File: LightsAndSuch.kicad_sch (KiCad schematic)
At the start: 13 parts, among them U1 STM32F205RBTx, U2 MAX98357A

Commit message: added secondary circuit
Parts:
- removed C10, C11, C12, C13, C14, C9: 100n, symbol Device:C
- removed C15: 1u, symbol Device:C
- removed C16: 4.7u', symbol Device:C
- removed C17: 0.1u, symbol Device:C
- removed C18: 10u, symbol Device:C
- removed LS1: Speaker, symbol Device:Speaker
- removed U1: STM32F205RBTx, Package_QFP:LQFP-64_10x10mm_P0.5mm, symbol MCU_ST_STM32F2:STM32F205RBTx
- removed U2: MAX98357A, Package_DFN_QFN:TQFN-16-1EP_3x3mm_P0.5mm_EP1.23x1.23mm, symbol Audio:MAX98357A
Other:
- added sheet Primary Sound Circuit (PrimarySoundCircuit.kicad_sch)
- added sheet Secondary Sound Circuit (SecondarySoundCircuit.kicad_sch)
- sheet TPS54202 ports: added none; removed 5V
- sheet TPS57A20 ports: added none; removed 3.3v, 5V

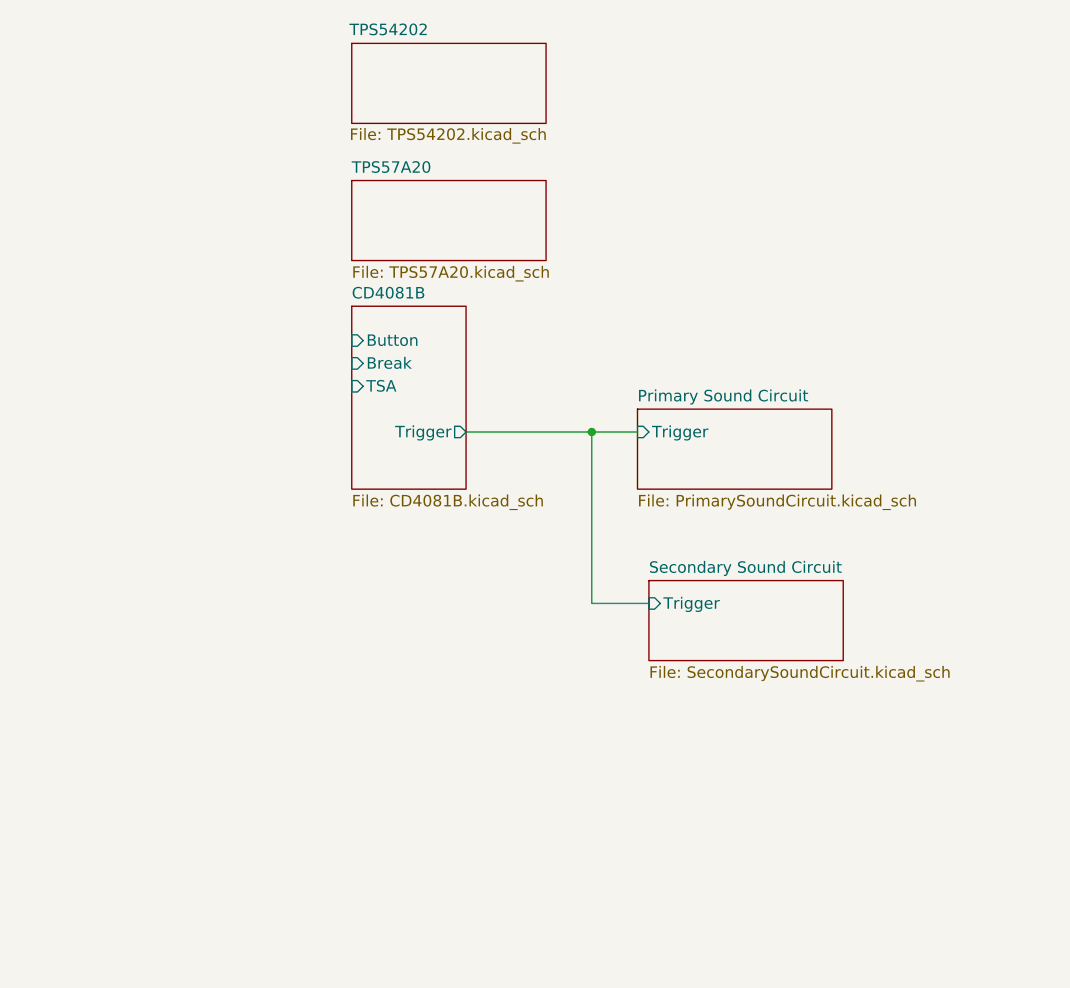
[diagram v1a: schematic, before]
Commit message: finished lights
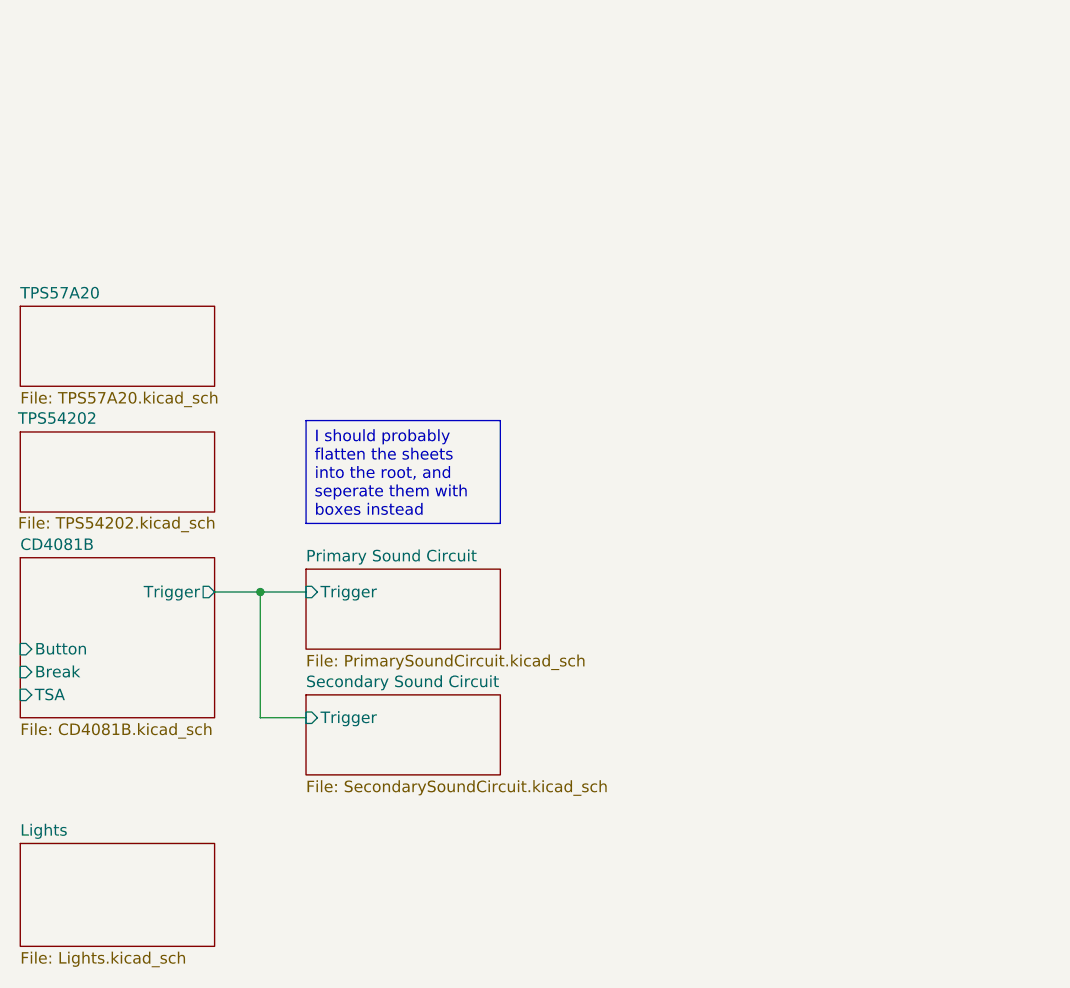
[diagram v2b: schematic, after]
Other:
- added sheet Lights (Lights.kicad_sch)
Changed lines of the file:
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@@
 	(generator_version "9.0")
 	(paper "A4")
+	(text_box "I should probably flatten the sheets into the root, and seperate them with boxes instead "
+		(exclude_from_sim no)
+		(at 76.2 59.69 0)
+		(size 21.59 11.43)
+		(margins 0.9525 0.9525 0.9525 0.9525)
+		(stroke
+			(width 0)
+			(type solid)
+		)
+		(fill
+			(type none)
+		)
+		(effects
+			(font
+				(size 1.27 1.27)
+			)
+			(justify left top)
+		)
+	)
 	(junction
-		(at 107.95 60.96)
+		(at 71.12 78.74)
 		(diameter 0)
 		(color 0 0 0 0)
@@
 	(wire
 		(pts
-			(xy 107.95 80.01) (xy 114.3 80.01)
+			(xy 71.12 92.71) (xy 76.2 92.71)
 		)
 		(stroke
@@
 	(wire
 		(pts
-			(xy 107.95 60.96) (xy 107.95 80.01)
+			(xy 66.04 78.74) (xy 71.12 78.74)
 		)
 		(stroke
@@
 	(wire
 		(pts
-			(xy 107.95 60.96) (xy 113.03 60.96)
+			(xy 71.12 92.71) (xy 71.12 78.74)
 		)
 		(stroke
@@
 	(wire
 		(pts
-			(xy 93.98 60.96) (xy 107.95 60.96)
+			(xy 71.12 78.74) (xy 76.2 78.74)
 		)
 		(stroke
@@
 	)
 	(sheet
-		(at 114.3 77.47)
+		(at 76.2 90.17)
 		(size 21.59 8.89)
 		(exclude_from_sim no)
@@
 		)
 		(property "Sheetname" "Secondary Sound Circuit"
-			(at 114.3 76.7584 0)
+			(at 76.2 89.4584 0)
 			(effects
 				(font
@@
 		)
 		(property "Sheetfile" "SecondarySoundCircuit.kicad_sch"
-			(at 114.3 86.9446 0)
+			(at 76.2 99.6446 0)
 			(effects
 				(font
@@
 		)
 		(pin "Trigger" input
-			(at 114.3 80.01 180)
+			(at 76.2 92.71 180)
 			(effects
 				(font
@@
 	)
 	(sheet
-		(at 81.28 46.99)
-		(size 12.7 20.32)
+		(at 44.45 74.93)
+		(size 21.59 17.78)
 		(exclude_from_sim no)
 		(in_bom yes)
@@
 		)
 		(property "Sheetname" "CD4081B"
-			(at 81.28 46.2784 0)
+			(at 44.45 74.2184 0)
 			(effects
 				(font
@@
 		)
 		(property "Sheetfile" "CD4081B.kicad_sch"
-			(at 81.28 67.8946 0)
+			(at 44.45 93.2946 0)
 			(effects
 				(font
@@
 		)
 		(pin "Button" input
-			(at 81.28 50.8 180)
+			(at 44.45 85.09 180)
 			(effects
 				(font
@@
 		)
 		(pin "Trigger" output
-			(at 93.98 60.96 0)
+			(at 66.04 78.74 0)
 			(effects
 				(font
@@
 		)
 		(pin "Break" input
-			(at 81.28 53.34 180)
+			(at 44.45 87.63 180)
 			(effects
 				(font
@@
 		)
 		(pin "TSA" input
-			(at 81.28 55.88 180)
+			(at 44.45 90.17 180)
 			(effects
 				(font
@@
 	)
 	(sheet
-		(at 81.28 17.78)
+		(at 44.45 60.96)
 		(size 21.59 8.89)
 		(exclude_from_sim no)
@@
 		)
 		(property "Sheetname" "TPS54202"
-			(at 81.026 17.018 0)
+			(at 44.196 60.198 0)
 			(effects
 				(font
@@
 		)
 		(property "Sheetfile" "TPS54202.kicad_sch"
-			(at 81.026 27.178 0)
+			(at 44.196 70.358 0)
 			(effects
 				(font
@@
 	)
 	(sheet
-		(at 81.28 33.02)
+		(at 44.45 46.99)
 		(size 21.59 8.89)
 		(exclude_from_sim no)
@@
 		)
 		(property "Sheetname" "TPS57A20"
-			(at 81.28 32.3084 0)
+			(at 44.45 46.2784 0)
 			(effects
 				(font
@@
 		)
 		(property "Sheetfile" "TPS57A20.kicad_sch"
-			(at 81.28 42.4946 0)
+			(at 44.45 56.4646 0)
 			(effects
 				(font
@@
 	)
 	(sheet
-		(at 113.03 58.42)
+		(at 76.2 76.2)
 		(size 21.59 8.89)
 		(exclude_from_sim no)
@@
 		)
 		(property "Sheetname" "Primary Sound Circuit"
-			(at 113.03 57.7084 0)
+			(at 76.2 75.4884 0)
 			(effects
 				(font
@@
 		)
 		(property "Sheetfile" "PrimarySoundCircuit.kicad_sch"
-			(at 113.03 67.8946 0)
+			(at 76.2 85.6746 0)
 			(effects
 				(font
@@
 		)
 		(pin "Trigger" input
-			(at 113.03 60.96 180)
+			(at 76.2 78.74 180)
 			(effects
 				(font
@@
 				)
 			)
+		)
+	)
+	(sheet
+		(at 44.45 106.68)
+		(size 21.59 11.43)
+		(exclude_from_sim no)
+		(in_bom yes)
+		(on_board yes)
+		(dnp no)
+		(fields_autoplaced yes)
+		(stroke
+			(width 0.1524)
+			(type solid)
+		)
+		(fill
+			(color 0 0 0 0.0000)
+		)
+		(property "Sheetname" "Lights"
+			(at 44.45 105.9684 0)
+			(effects
+				(font
+					(size 1.27 1.27)
+				)
+				(justify left bottom)
+			)
+		)
+		(property "Sheetfile" "Lights.kicad_sch"
+			(at 44.45 118.6946 0)
+			(effects
+				(font
+					(size 1.27 1.27)
+				)
+				(justify left top)
+			)
+		)
+		(instances
+			(project "LightsAndSuch"
+				(path "/f2987657-b7e0-480f-b307-23af9e47acd8"
+					(page "7")
+				)
+			)

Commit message: flattened file into one sheet
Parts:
- added 0.1u: Cboot, symbol Device:C_Small
- added C1: 10u, symbol Device:C_Small
- added C10, C11, C12, C13, C14, C9: 100n, symbol Device:C
- added C15, C2, C7, C8: 1u, symbol Device:C
- added C16: 4.7u', symbol Device:C
- added C17, C19, C23, C25: 0.1u, symbol Device:C
- added C18, C22, C24: 10u, symbol Device:C
- added C20: 0.01u, symbol Device:C
- added C21, C26, C27: C, symbol Device:C
- added C3, C5: 22u, symbol Device:C
- added C4: 0.1u, symbol Device:C_Small
- added C6: 75p, symbol Device:C
- added D1, D2, D3: LED, symbol Device:LED
- added L1: 20u, symbol Device:L_Iron
- added LS1: Speaker, symbol Device:Speaker
- added LS2, LS3: MSO206NR, symbol Device:Speaker
- added Q1: AO3400A, Package_TO_SOT_SMD:SOT-23, symbol Transistor_FET:AO3400A
- added Q2: NPN, symbol Simulation_SPICE:NPN
- added R1, R10, R11, R12, R13, R14, R15, R16, R17, R3, R9: R, symbol Device:R
- added R2: 100k, symbol Device:R_Small
- added R4: 100k, symbol Device:R
- added R5: 13.3k, symbol Device:R_Small
- added R6: 5.23k, symbol Device:R_Small
- added R7: 13.7k, symbol Device:R_Small
- added R8: 100, symbol Device:R
- added U1: STM32F205RBTx, Package_QFP:LQFP-64_10x10mm_P0.5mm, symbol MCU_ST_STM32F2:STM32F205RBTx
- added U2: MAX98357A, Package_DFN_QFN:TQFN-16-1EP_3x3mm_P0.5mm_EP1.23x1.23mm, symbol Audio:MAX98357A
- added U3: TPS54202DDC, Package_TO_SOT_SMD:SOT-23-6, symbol Regulator_Switching:TPS54202DDC
- added U4: TPS7A20xxxDQN, Package_SON:Texas_X2SON-4_1x1mm_P0.65mm, symbol Regulator_Linear:TPS7A20xxxDQN
- added U5: CD4081BM, D14, symbol CD4081B:CD4081BM
- added U6, U7, U8: LM555xM, Package_SO:SOIC-8_3.9x4.9mm_P1.27mm, symbol Timer:LM555xM
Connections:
- new net: R10.2, R9.1, U7.7 (DIS)
- new net: 0.1u.2, L1.1, U3.2 (SW)
- new net: C6.2, R2.2, R5.1, U3.4 (FB)
- new net: 0.1u.1, U3.6 (BOOT)
- new net: Q2.2 (B), R15.1
- new net: R1.2, U6.7 (DIS)
- new net: D2.2 (A), U8.3 (Q)
- new net: C27.1, U8.5 (CV)
- new net: R13.2, R14.1, U8.7 (DIS)
- new net: R8.1, U6.3 (Q)
- new net: Q1.1 (G), R4.1, R8.2
- new net: D1.2 (A), U7.3 (Q)
- new net: Q2.1 (C), R16.1, R17.2
- new net: U1.34 (PB13), U2.16 (BCLK)
- new net: U1.36 (PB15), U2.1 (DIN)
- new net: U1.62 (PB9), U2.14 (LRCLK)
- new net: LS2.2, LS3.2, Q1.3 (D)
- new net: D3.2 (A), R17.1
- new net: C26.1, U7.5 (CV)
- new net: U5.3 (J), U5.5 (C)
- new net: R7.1, U5.4 (K)
- new net: C20.1, U6.5 (CV)
- new net: LS1.1, U2.9 (OUTP)
- new net: LS1.2, U2.10 (OUTN)
- new net +12V: C1.1, C4.1, R10.1, R13.1, R16.2, U3.3 (VIN), U5.14 (VDD), U7.8 (VCC), U8.8 (VCC)
- new net +3.3V: C10.1, C11.1, C12.1, C13.1, C14.2, C15.2, C16.1, C8.1, C9.1, U1.1 (VBAT), U1.13 (VDDA), U1.19 (VDD), U1.32 (VDD), U1.48 (VDD), U1.64 (VDD), U2.4 (~{SD_MODE}), U4.1 (OUT)
- new net +5V: C17.2, C18.2, C19.1, C19.2, C2.1, C2.2, C21.2, C22.1, C22.2, C23.1, C23.2, C24.1, C24.2, C25.1, C25.2, C3.1, C5.1, C6.1, C7.1, L1.2, LS2.1, LS3.1, R1.1, R2.1, U2.2 (GAIN_SLOT), U2.7 (VDD), U2.8 (VDD), U4.3 (EN), U4.4 (IN), U6.6 (THR), U6.8 (VCC)
- new net Break: U5.2 (B)
- new net Button: U5.6 (D)
- new net FAULT: R12.1, R15.2, U8.4 (R)
- new net GND: C1.2, C10.2, C11.2, C12.2, C13.2, C14.1, C15.1, C16.2, C17.1, C18.1, C20.2, C21.1, C26.2, C27.2, C3.2, C4.2, C5.2, C7.2, C8.2, C9.2, D1.1 (K), D2.1 (K), D3.1 (K), Q1.2 (S), Q2.3 (E), R11.2, R12.2, R14.2, R3.1, R4.2, R5.2, R6.2, R9.2, U1.12 (VSSA), U1.18 (VSS), U1.63 (VSS), U2.11 (GND), U2.15 (GND), U2.17 (PAD), U2.3 (GND), U3.1 (GND), U4.2 (GND), U4.5 (Pad), U5.7 (VSS), U6.1 (GND), U6.4 (R), U7.1 (GND), U7.2 (TR), U7.6 (THR), U8.1 (GND), U8.2 (TR), U8.6 (THR)
- new net HV_Enable: R11.1, U7.4 (R)
- new net TSA: U5.1 (A)
- new net Trigger: R3.2, R6.1, R7.2, U1.8 (PC0), U6.2 (TR)
- no-connect marks 0 -> 1
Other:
- removed sheet CD4081B
- removed sheet Lights
- removed sheet Primary Sound Circuit
- removed sheet Secondary Sound Circuit
- removed sheet TPS54202
- removed sheet TPS57A20
- note added: "Lights"
- note added: "Logic"
- note added: "Power"
- note added: "Primary Sound Circuit"
- note added: "Secondary Sound Circuit"

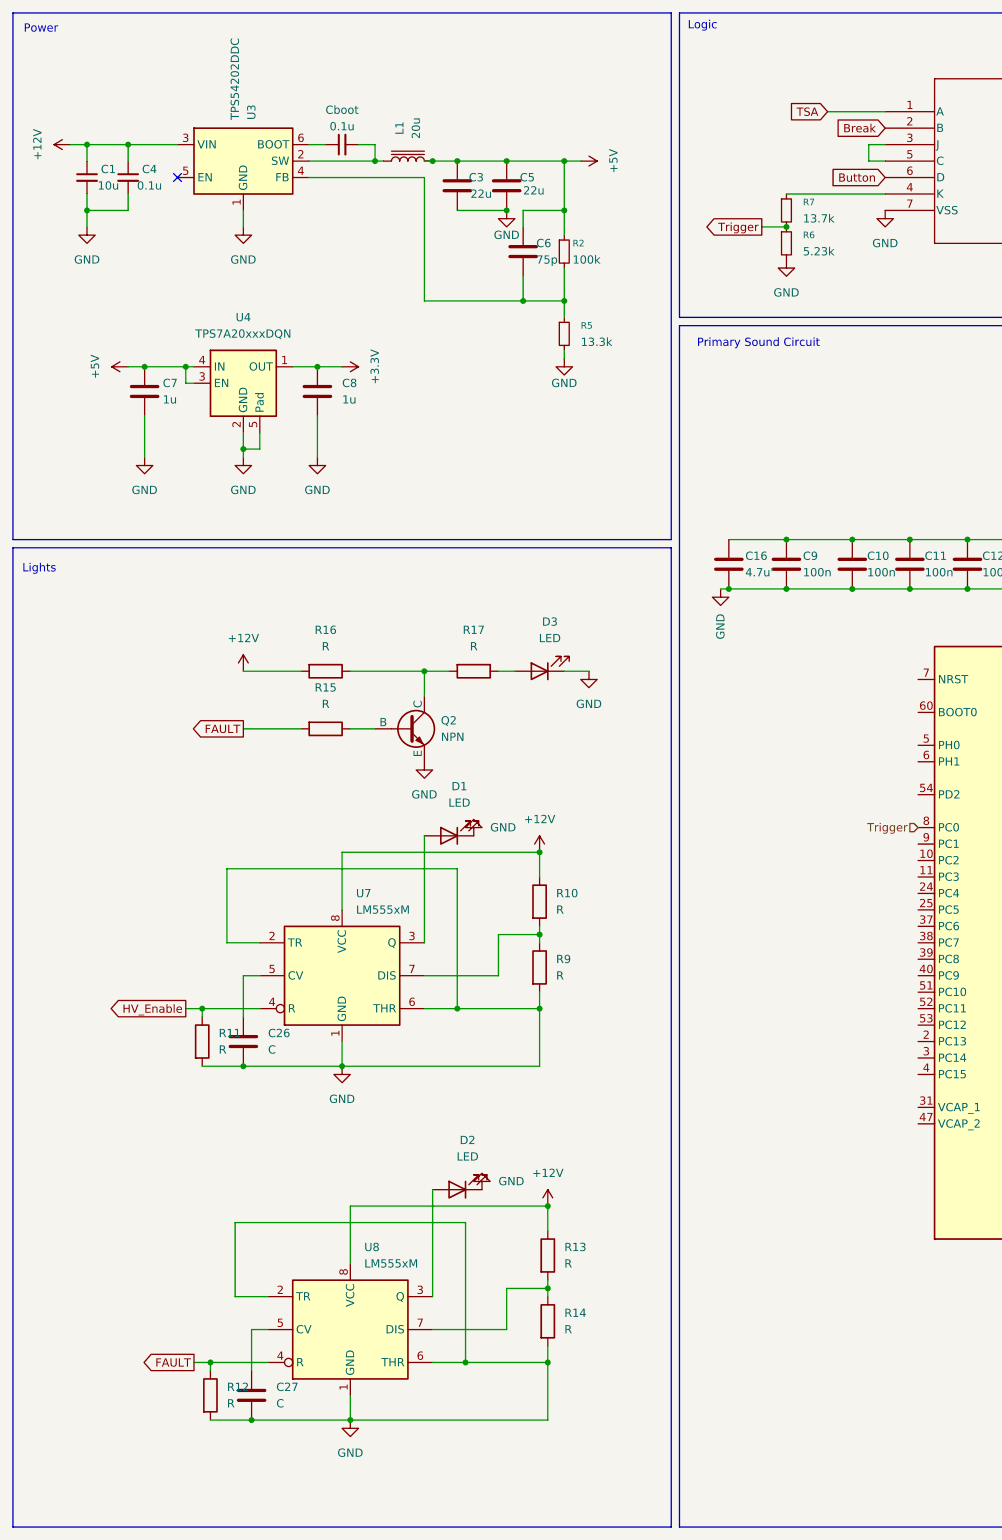
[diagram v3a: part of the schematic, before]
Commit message: added missing capacitor for the 555
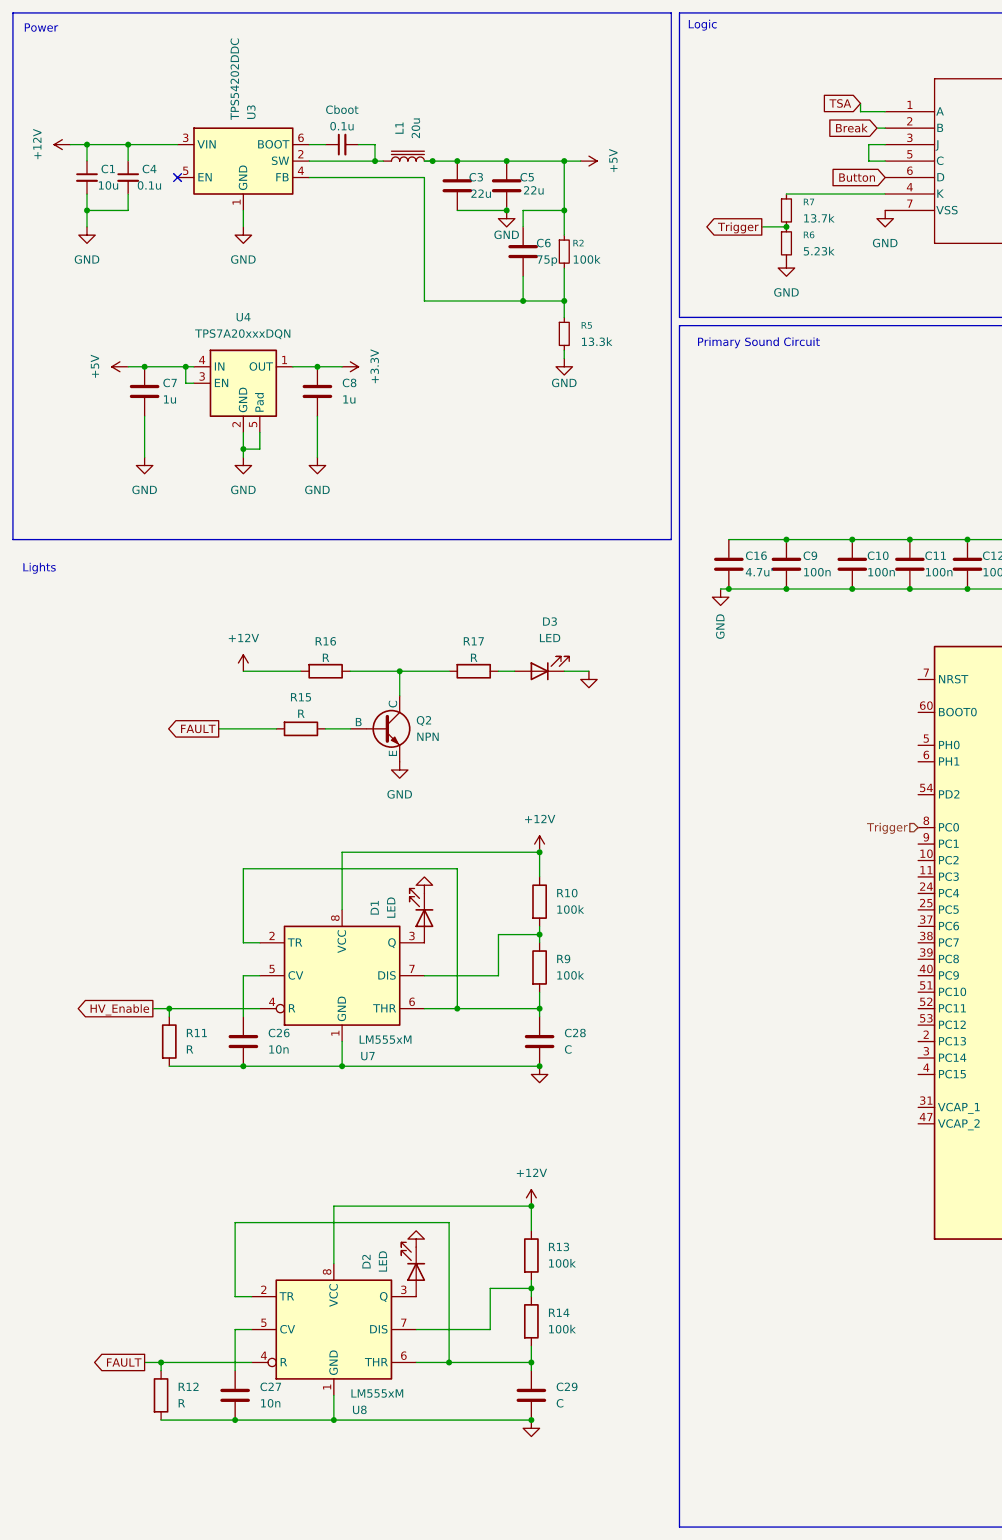
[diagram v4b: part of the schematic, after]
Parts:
- added C28, C29: C, symbol Device:C
- C26, C27: value C -> 10n
- R10, R13, R14, R9: value R -> 100k
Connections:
- net GND: now also C28.2, C29.2; no longer R14.2, R9.2, U7.2 (TR), U7.6 (THR), U8.2 (TR), U8.6 (THR)
- new net: C28.1, R9.2, U7.2 (TR), U7.6 (THR)
- new net: C29.1, R14.2, U8.2 (TR), U8.6 (THR)
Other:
- moved on the sheet: D1, Q2, R11, R15

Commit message: most values set in and pull up resistors
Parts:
- added R18, R19, R20: 10k, symbol Device:R
- C21: value C -> 10u
- C26: value 10n -> 0.1u
- C27: value 10n -> 100u
- C28: value C -> 0.1u
- C29: value C -> 100u
- R1: value R -> 200k
- R10, R13: value 100k -> 3.6k
- R11, R12, R3: value R -> 10k
- R14, R9: value 100k -> 10k
- R8: value 100 -> 100k
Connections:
- net +12V: no longer R10.1, R13.1, U7.8 (VCC), U8.8 (VCC)
- net +5V: now also C26.1, C28.1, R14.1, R9.1, U7.8 (VCC), U8.8 (VCC)
- net Break: now also R19.2
- net Button: now also R20.2
- net FAULT: now also R11.2, U7.4 (R); no longer R12.1, U8.4 (R)
- net GND: now also C27.1, C29.1, R11.1, R12.1, R18.1, R19.1, R20.1; no longer C27.2, C29.2, R11.2, R12.2
- net TSA: now also R18.2
- net at U8.5 (CV): no longer C27.1
- net at U7.5 (CV): no longer C26.1
- removed net HV_Enable: R11.1, U7.4 (R)
- new net: R13.2, U8.2 (TR)
- new net: C29.2, R13.1, U8.6 (THR)
- new net: R14.2, U8.7 (DIS)
- new net: C27.2, R10.1, U7.6 (THR)
- new net: R9.2, U7.7 (DIS)
- new net: R10.2, U7.2 (TR)
- new net HV: R12.2, U8.4 (R)
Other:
- moved on the sheet: C21, C3, D3, Q2, R15, R16, R17, R3, R4, R6, R7, U7

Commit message: added mosfets to account for 555 current output, sized low side driver for green light
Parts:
- removed D2: LED, symbol Device:LED
- removed Q2: NPN, symbol Simulation_SPICE:NPN
- removed R15, R16, R17: R, symbol Device:R
- added D4: LED, symbol Device:LED
- added Q2, Q3, Q4: AO3400A, Package_TO_SOT_SMD:SOT-23, symbol Transistor_FET:AO3400A
- added R15: 100k, symbol Device:R_Small
- added R21, R22: 10k, symbol Device:R_Small
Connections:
- net FAULT is gone; now on net Fault: R11.2, U7.4 (R)
- net TSA is gone; now on net HV: R18.2, U5.1 (A)
- net +12V: now also C26.2, C28.2, D1.2 (A), D3.2 (A), D4.2 (A), Q3.3 (D)
- net GND: now also Q3.2 (S), Q4.2 (S), R15.1, R21.2, R22.2; no longer C26.2, C28.2, D1.1 (K)
- net at U7.3 (Q): now also Q2.1 (G); no longer D1.2 (A)
- net at U8.3 (Q): now also Q4.1 (G)
- net at C27.2, R10.1, U7.6 (THR): now also Q2.2 (S)
- net Fault: now reaches U5.11 (M)
- net Fault: now also Q3.1 (G), R15.2
- net IMD_Fault: now reaches U5.12 (G)
- net IMD_Fault: now also R22.1
- net BMS_Fault: now reaches U5.13 (H)
- net BMS_Fault: now also R21.1
- new net: D1.1 (K), Q2.3 (D)
- new net: D4.1 (K), Q4.3 (D)
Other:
- moved on the sheet: C26, C27, C28, C29, D3, R10, R11, R12, R13, R14, R9, U7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

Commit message: SWD connector
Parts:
- added J1: Conn_ARM_SWD_TagConnect_TC2030, Connector:Tag-Connect_TC2030-IDC-FP_2x03_P1.27mm_Vertical, symbol Connector:Conn_ARM_SWD_TagConnect_TC2030
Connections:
- net +12V: no longer D3.2 (A), Q3.3 (D)
- net +3.3V: now also J1.1 (VCC)
- net GND: now also J1.5 (GND)
- net at U1.46 (PA13): now also J1.2 (SWDIO)
- net at U1.49 (PA14): now also J1.4 (SWCLK)
- net at U1.55 (PB3): now also J1.6 (SWO)
- net at U1.56 (PB4): now also J1.3 (~{RESET})
- new net: D3.2 (A), Q3.3 (D)
